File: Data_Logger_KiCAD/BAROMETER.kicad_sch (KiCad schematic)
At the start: 0 parts

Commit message: Imported Barometer Into Main Branch
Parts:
- added C13, C15: 100 nF, symbol Device:C
- added C14, C16: 1 uF, symbol Device:C
- added R5: 10k, symbol Device:R
- added U5: MS560702BA03-50, MS56:SON8_MS5611_TEC, symbol MS560702BA03-50:MS560702BA03-50
- added U6: BMP390L, BMP390L:XDCR_BMP390L, symbol BMP390L:BMP390L
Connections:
- new net: R5.1, U5.5 (~{CSB__1})
- new net +3.3V: C13.1, C14.1, C15.1, C16.1, R5.2, U5.1 (VDD), U6.1 (VDDIO), U6.10 (VDD)
- new net CSB_BMP: U6.6 (~{CS})
- new net CSB_MS: U5.4 (~{CSB})
- new net GND: C13.2, C14.2, C15.2, C16.2, U5.2 (PS), U5.3 (GND), U6.3 (VSS/GND), U6.8 (VSS/GND), U6.9 (VSS/GND)
- new net SCK: U5.8 (SCLK), U6.2 (SCK/SCL)
- new net SDI: U5.7 (SDI/SDA), U6.4 (SDI/SDO/SDA)
- new net SDO: U5.6 (SDO), U6.5 (SDO/DNC/SA0)
- no-connect marks 0 -> 1
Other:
- note added: "4-wire SPI connection"
- note added: "BMP390"
- note added: "Decoupling: 100nF + 1µF ceramic capacitors between 3.3V and GND"
- note added: "General Notes: - Changed to 4-wire SPI connection - Added consistent labels - Added a 1 uF capacitor (as done for BMP390)"
- note added: "General Notes: - VDD and VDDIO can share the same 3.3V rail - Use short traces for SPI signals for reliable communication - Place decoupling capacitors as close as possible to BMP390L pins - All pins not shown in SPI diagram (NC or reserved) should remain unconnected - The 1 uF capacitor is optional, but recommended for noise filtration"
- note added: "MS5607"
- note added: "PS = GND -> SPI mode"
- note added: "Pull CSB_1 high (not used)"
- note added: "SPI Interface: SCK → SPI Clock (connect to ESP32-S3 SCLK) SDI → SPI MOSI (data from MCU to sensor) SDO → SPI MISO (data from sensor to MCU) CS → Chip Select (active low, connect to any GPIO) INT → Optional interrupt for data ready (connect to GPIO if needed) SPI Mode 0 recommended (CPOL=0, CPHA=0)"
- note added: "Vss = GND (Pins 3, 8, and 9)"

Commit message: Sub-schematics Generated
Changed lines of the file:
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@@
 		)
 	)
-	(global_label "SCK"
-		(shape input)
-		(at 35.56 121.92 180)
-		(fields_autoplaced yes)
+	(hierarchical_label "SDO"
+		(shape output)
+		(at 29.21 127 180)
 		(effects
 			(font
@@
 			(justify right)
 		)
-		(property "Intersheetrefs" "${INTERSHEET_REFS}"
-			(at 28.8253 121.92 0)
-			(effects
-				(font
-					(size 1.27 1.27)
-				)
-				(justify right)
-				(hide yes)
-			)
-		)
 	)
-	(global_label "CSB_BMP"
+	(hierarchical_label "SCK"
 		(shape input)
-		(at 40.64 116.84 180)
-		(fields_autoplaced yes)
+		(at 35.56 121.92 180)
 		(effects
 			(font
@@
 			(justify right)
 		)
-		(property "Intersheetrefs" "${INTERSHEET_REFS}"
-			(at 28.9463 116.84 0)
-			(effects
-				(font
-					(size 1.27 1.27)
-				)
-				(justify right)
-				(hide yes)
-			)
-		)
 	)
-	(global_label "CSB_MS"
+	(hierarchical_label "SDI"
 		(shape input)
-		(at 45.72 41.91 180)
-		(fields_autoplaced yes)
+		(at 41.91 54.61 180)
 		(effects
 			(font
@@
 			(justify right)
 		)
-		(property "Intersheetrefs" "${INTERSHEET_REFS}"
-			(at 35.3568 41.91 0)
-			(effects
-				(font
-					(size 1.27 1.27)
-				)
-				(justify right)
-				(hide yes)
-			)
-		)
 	)
-	(global_label "SDI"
+	(hierarchical_label "SDI"
 		(shape input)
 		(at 35.56 124.46 180)
-		(fields_autoplaced yes)
 		(effects
 			(font
@@
 			(justify right)
 		)
-		(property "Intersheetrefs" "${INTERSHEET_REFS}"
-			(at 29.4905 124.46 0)
-			(effects
-				(font
-					(size 1.27 1.27)
-				)
-				(justify right)
-				(hide yes)
-			)
-		)
 	)
-	(global_label "SDI"
+	(hierarchical_label "CSB_BMP"
 		(shape input)
-		(at 41.91 54.61 180)
-		(fields_autoplaced yes)
+		(at 40.64 116.84 180)
 		(effects
 			(font
@@
 			(justify right)
 		)
-		(property "Intersheetrefs" "${INTERSHEET_REFS}"
-			(at 35.8405 54.61 0)
-			(effects
-				(font
-					(size 1.27 1.27)
-				)
-				(justify right)
-				(hide yes)
+	)
+	(hierarchical_label "SDO"
+		(shape output)
+		(at 90.17 46.99 0)
+		(effects
+			(font
+				(size 1.27 1.27)
 			)
+			(justify left)
 		)
 	)
-	(global_label "SDO"
-		(shape output)
-		(at 29.21 127 180)
-		(fields_autoplaced yes)
+	(hierarchical_label "SCK"
+		(shape input)
+		(at 41.91 49.53 180)
 		(effects
 			(font
@@
 			(justify right)
 		)
-		(property "Intersheetrefs" "${INTERSHEET_REFS}"
-			(at 22.4148 127 0)
-			(effects
-				(font
-					(size 1.27 1.27)
-				)
-				(justify right)
-				(hide yes)
-			)
-		)
 	)
-	(global_label "SCK"
+	(hierarchical_label "CSB_MS"
 		(shape input)
-		(at 41.91 49.53 180)
-		(fields_autoplaced yes)
+		(at 45.72 41.91 180)
 		(effects
 			(font
@@
 			(justify right)
 		)
-		(property "Intersheetrefs" "${INTERSHEET_REFS}"
-			(at 35.1753 49.53 0)
-			(effects
-				(font
-					(size 1.27 1.27)
-				)
-				(justify right)
-				(hide yes)
-			)
-		)
 	)
-	(global_label "SDO"
-		(shape output)
-		(at 90.17 46.99 0)
-		(fields_autoplaced yes)
-		(effects
-			(font
-				(size 1.27 1.27)
-			)
-			(justify left)
-		)
-		(property "Intersheetrefs" "${INTERSHEET_REFS}"
-			(at 96.9652 46.99 0)
-			(effects
-				(font
-					(size 1.27 1.27)
-				)
-				(justify left)
-				(hide yes)
-			)
-		)
-	)

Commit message: Radio Layout V1.0
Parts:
- removed C13: 100 nF, symbol Device:C
- removed C14: 1 uF, symbol Device:C
- removed R5: 10k, symbol Device:R
- removed U5: MS560702BA03-50, MS56:SON8_MS5611_TEC, symbol MS560702BA03-50:MS560702BA03-50
- added C3: 1 uF, Capacitor_SMD:C_0402_1005Metric, symbol Device:C
- added C4: 100 nF, Capacitor_SMD:C_0402_1005Metric, symbol Device:C
- added U2: MS5607-02BA, Package_LGA:LGA-8_3x5mm_P1.25mm, symbol Sensor_Pressure:MS5607-02BA
- C15: value 100 nF -> 100n; footprint (none) -> Capacitor_SMD:C_0402_1005Metric
- C16: value 1 uF -> 1u; footprint (none) -> Capacitor_SMD:C_0402_1005Metric
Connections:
- net +3.3V: now also C3.2, C4.1, U2.1 (VDD)
- net CSB_MS: now also U2.4 (CSB), U2.5 (CSB)
- net GND: now also C3.1, C4.2, U2.2 (PS), U2.3 (GND)
- net SCK: now also U2.8 (SCLK)
- net SDI: now also U2.7 (SDI/SDA)
- net SDO: now also U2.6 (SDO)

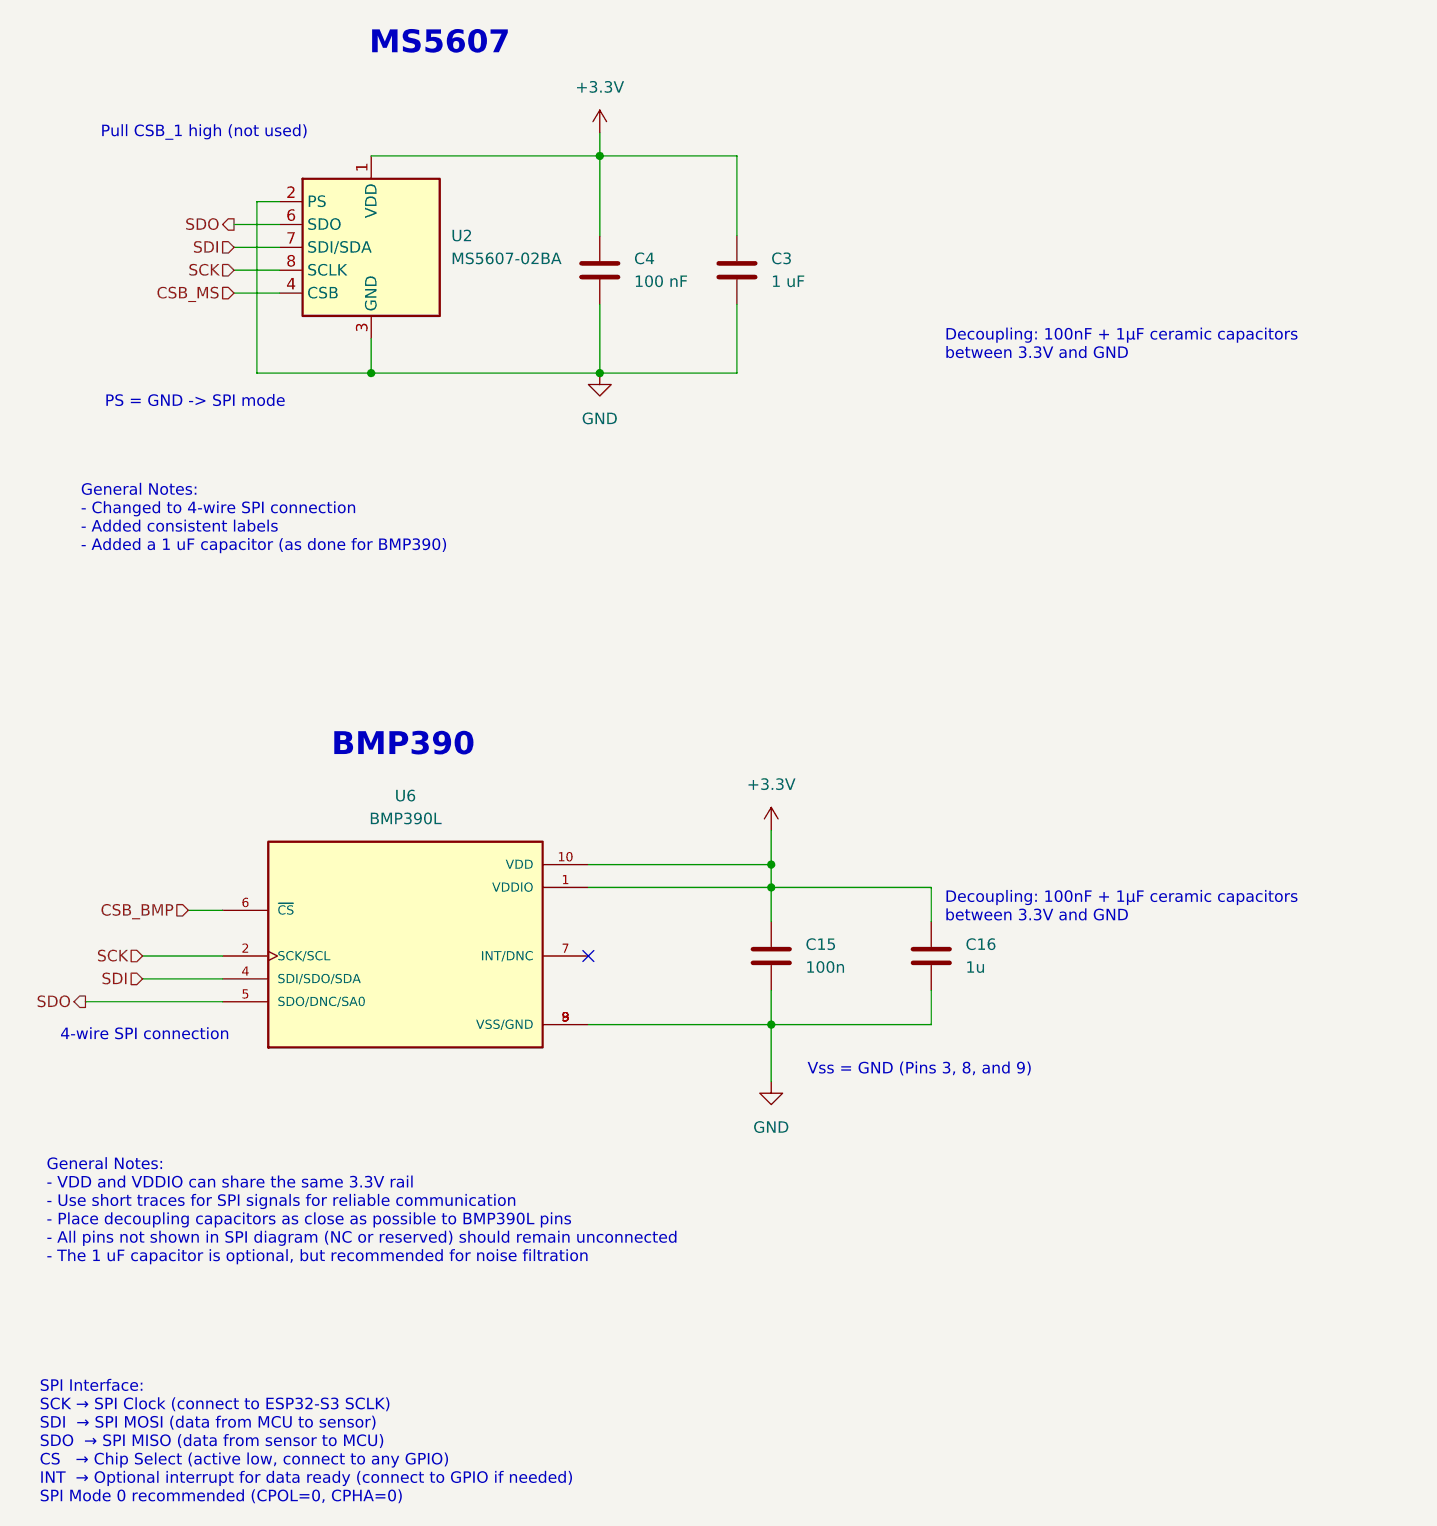
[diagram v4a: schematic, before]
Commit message: Aggregated sub schematics into single primary schematic
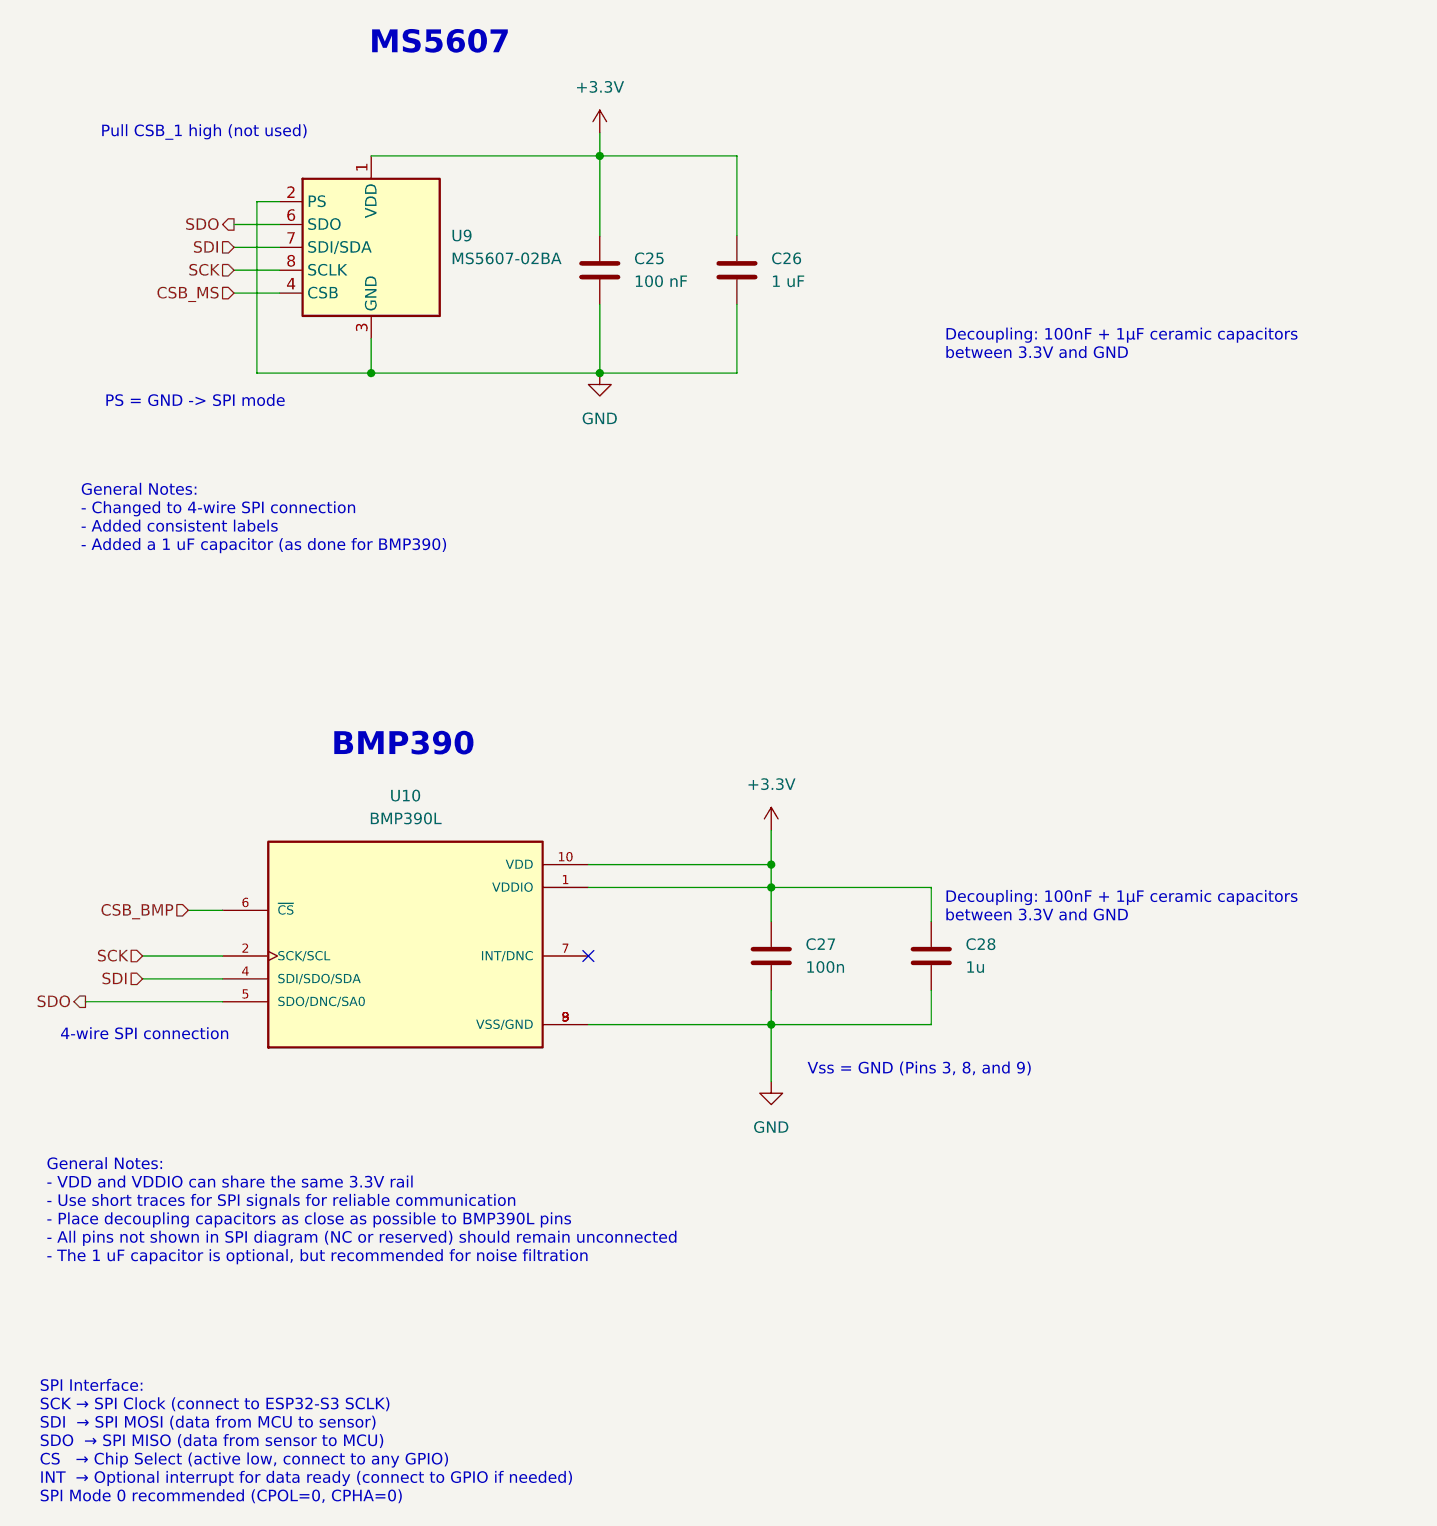
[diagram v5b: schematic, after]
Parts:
- renumbered C4 to C25, C3 to C26, C15 to C27, C16 to C28, U6 to U10, U2 to U9
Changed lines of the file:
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@@
 		(dnp no)
 		(fields_autoplaced yes)
-		(property "Reference" "#PWR023"
+		(property "Reference" "#PWR049"
 			(at 105.41 142.24 0)
 			(effects
@@
 		(instances
 			(project "Data_Logger_Board"
-				(path "/db968e42-3ace-4cc9-9096-9d8f48135c40/6de4bf02-03b0-4601-a6b2-a0bf99e05925"
-					(reference "#PWR023")
+				(path "/db968e42-3ace-4cc9-9096-9d8f48135c40/795ab2be-9db7-4254-b05c-ac2b60177344/909dd632-2a0f-4e55-b8e6-044af71dac19"
+					(reference "#PWR049")
 					(unit 1)
 				)
@@
 		(on_board yes)
 		(dnp no)
-		(property "Reference" "#PWR06"
+		(property "Reference" "#PWR046"
 			(at 86.36 34.29 0)
 			(effects
@@
 		(instances
 			(project "Data_Logger_Board"
-				(path "/db968e42-3ace-4cc9-9096-9d8f48135c40/6de4bf02-03b0-4601-a6b2-a0bf99e05925"
-					(reference "#PWR06")
+				(path "/db968e42-3ace-4cc9-9096-9d8f48135c40/795ab2be-9db7-4254-b05c-ac2b60177344/909dd632-2a0f-4e55-b8e6-044af71dac19"
+					(reference "#PWR046")
 					(unit 1)
 				)
@@
 		(dnp no)
 		(fields_autoplaced yes)
-		(property "Reference" "C15"
+		(property "Reference" "C27"
 			(at 109.22 120.6499 0)
 			(effects
@@
 		(instances
 			(project "Data_Logger_Board"
-				(path "/db968e42-3ace-4cc9-9096-9d8f48135c40/6de4bf02-03b0-4601-a6b2-a0bf99e05925"
-					(reference "C15")
+				(path "/db968e42-3ace-4cc9-9096-9d8f48135c40/795ab2be-9db7-4254-b05c-ac2b60177344/909dd632-2a0f-4e55-b8e6-044af71dac19"
+					(reference "C27")
 					(unit 1)
 				)
@@
 		(dnp no)
 		(fields_autoplaced yes)
-		(property "Reference" "C16"
+		(property "Reference" "C28"
 			(at 127 120.6499 0)
 			(effects
@@
 		(instances
 			(project "Data_Logger_Board"
-				(path "/db968e42-3ace-4cc9-9096-9d8f48135c40/6de4bf02-03b0-4601-a6b2-a0bf99e05925"
-					(reference "C16")
+				(path "/db968e42-3ace-4cc9-9096-9d8f48135c40/795ab2be-9db7-4254-b05c-ac2b60177344/909dd632-2a0f-4e55-b8e6-044af71dac19"
+					(reference "C28")
 					(unit 1)
 				)
@@
 		(dnp no)
 		(fields_autoplaced yes)
-		(property "Reference" "C4"
+		(property "Reference" "C25"
 			(at 90.17 44.4499 0)
 			(effects
@@
 		(instances
 			(project "Data_Logger_Board"
-				(path "/db968e42-3ace-4cc9-9096-9d8f48135c40/6de4bf02-03b0-4601-a6b2-a0bf99e05925"
-					(reference "C4")
+				(path "/db968e42-3ace-4cc9-9096-9d8f48135c40/795ab2be-9db7-4254-b05c-ac2b60177344/909dd632-2a0f-4e55-b8e6-044af71dac19"
+					(reference "C25")
 					(unit 1)
 				)
@@
 		(dnp no)
 		(fields_autoplaced yes)
-		(property "Reference" "C3"
+		(property "Reference" "C26"
 			(at 105.41 44.4499 0)
 			(effects
@@
 		(instances
 			(project "Data_Logger_Board"
-				(path "/db968e42-3ace-4cc9-9096-9d8f48135c40/6de4bf02-03b0-4601-a6b2-a0bf99e05925"
-					(reference "C3")
+				(path "/db968e42-3ace-4cc9-9096-9d8f48135c40/795ab2be-9db7-4254-b05c-ac2b60177344/909dd632-2a0f-4e55-b8e6-044af71dac19"
+					(reference "C26")
 					(unit 1)
 				)
@@
 		(dnp no)
 		(fields_autoplaced yes)
-		(property "Reference" "U2"
+		(property "Reference" "U9"
 			(at 69.85 41.9099 0)
 			(effects
@@
 		)
 		(instances
-			(project ""
-				(path "/db968e42-3ace-4cc9-9096-9d8f48135c40/6de4bf02-03b0-4601-a6b2-a0bf99e05925"
-					(reference "U2")
+			(project "Data_Logger_Board"
+				(path "/db968e42-3ace-4cc9-9096-9d8f48135c40/795ab2be-9db7-4254-b05c-ac2b60177344/909dd632-2a0f-4e55-b8e6-044af71dac19"
+					(reference "U9")
 					(unit 1)
 				)
@@
 		(dnp no)
 		(fields_autoplaced yes)
-		(property "Reference" "#PWR05"
+		(property "Reference" "#PWR047"
 			(at 86.36 63.5 0)
 			(effects
@@
 		(instances
 			(project "Data_Logger_Board"
-				(path "/db968e42-3ace-4cc9-9096-9d8f48135c40/6de4bf02-03b0-4601-a6b2-a0bf99e05925"
-					(reference "#PWR05")
+				(path "/db968e42-3ace-4cc9-9096-9d8f48135c40/795ab2be-9db7-4254-b05c-ac2b60177344/909dd632-2a0f-4e55-b8e6-044af71dac19"
+					(reference "#PWR047")
 					(unit 1)
 				)
@@
 		(on_board yes)
 		(dnp no)
-		(property "Reference" "U6"
+		(property "Reference" "U10"
 			(at 64.77 104.14 0)
 			(effects
@@
 		(instances
 			(project "Data_Logger_Board"
-				(path "/db968e42-3ace-4cc9-9096-9d8f48135c40/6de4bf02-03b0-4601-a6b2-a0bf99e05925"
-					(reference "U6")
+				(path "/db968e42-3ace-4cc9-9096-9d8f48135c40/795ab2be-9db7-4254-b05c-ac2b60177344/909dd632-2a0f-4e55-b8e6-044af71dac19"
+					(reference "U10")
 					(unit 1)
 				)
@@
 		(dnp no)
 		(fields_autoplaced yes)
-		(property "Reference" "#PWR022"
+		(property "Reference" "#PWR048"
 			(at 105.41 111.76 0)
 			(effects
@@
 		(instances
 			(project "Data_Logger_Board"
-				(path "/db968e42-3ace-4cc9-9096-9d8f48135c40/6de4bf02-03b0-4601-a6b2-a0bf99e05925"
-					(reference "#PWR022")
-					(unit 1)
-				)
+				(path "/db968e42-3ace-4cc9-9096-9d8f48135c40/795ab2be-9db7-4254-b05c-ac2b60177344/909dd632-2a0f-4e55-b8e6-044af71dac19"
+					(reference "#PWR048")
+					(unit 1)
+				)
